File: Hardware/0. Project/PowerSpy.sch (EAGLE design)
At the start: 86 parts, among them CN1 Mini-Fit 4T, IC1 CP2102N-A01-GQFN28, T1 SS8050, T2 SS8050, U1 MCP6021, U2 MCP6024, U3 ADS1115IDGST, U4 HLK-PM01, U5 NCP1117ST33T3G, U6 ESP32-WROOM-32D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

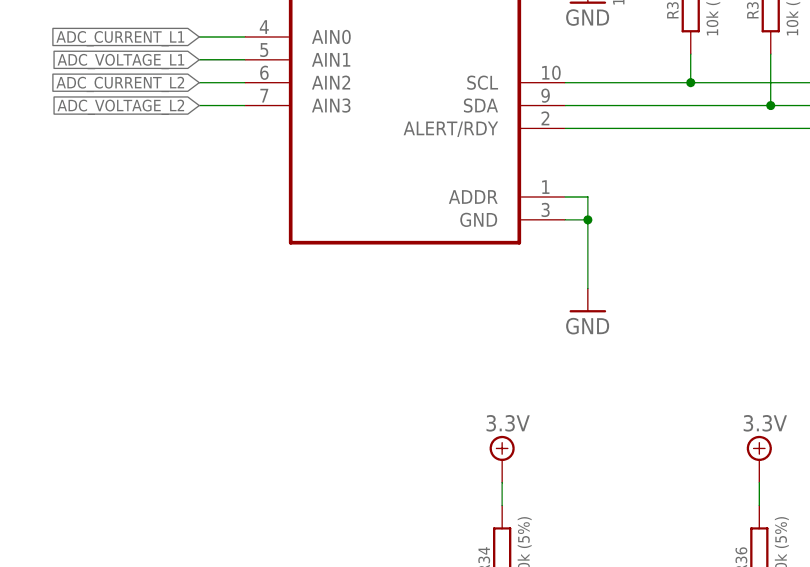
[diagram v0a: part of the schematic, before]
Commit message: ADS1115 7-bits slave address added to schematic
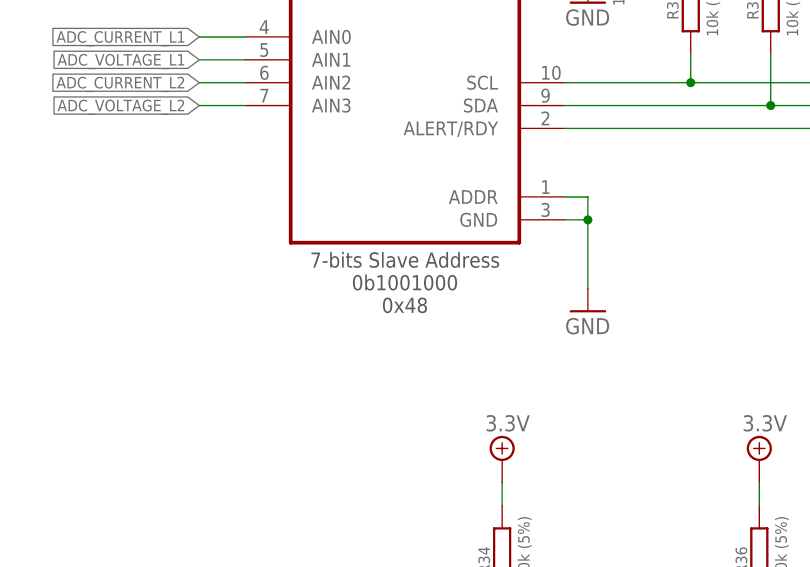
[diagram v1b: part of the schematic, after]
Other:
- note added: "7-bits Slave Address 0b1001000 0x48"
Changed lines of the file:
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@@
 <setting verticaltext="up"/>
 </settings>
-<grid distance="0.1" unitdist="inch" unit="inch" style="lines" multiple="1" display="no" altdistance="0.01" altunitdist="inch" altunit="inch"/>
+<grid distance="0.05" unitdist="inch" unit="inch" style="lines" multiple="1" display="no" altdistance="0.01" altunitdist="inch" altunit="inch"/>
 <layers>
 <layer number="1" name="Top" color="4" fill="1" visible="no" active="no"/>
@@
 <text x="22.86" y="170.18" size="1.778" layer="97">Máx. 1,65V</text>
 <text x="120.65" y="170.18" size="1.778" layer="97">Máx. 1,65V</text>
+<text x="215.9" y="76.2" size="1.6764" layer="97" font="vector" ratio="5" align="center">7-bits Slave Address
+0b1001000
+0x48</text>
 </plain>
 <instances>
